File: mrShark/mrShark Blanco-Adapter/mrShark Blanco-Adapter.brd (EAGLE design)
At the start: 26 x 31 mm, 1 part, among them CON1 DF12-20DS

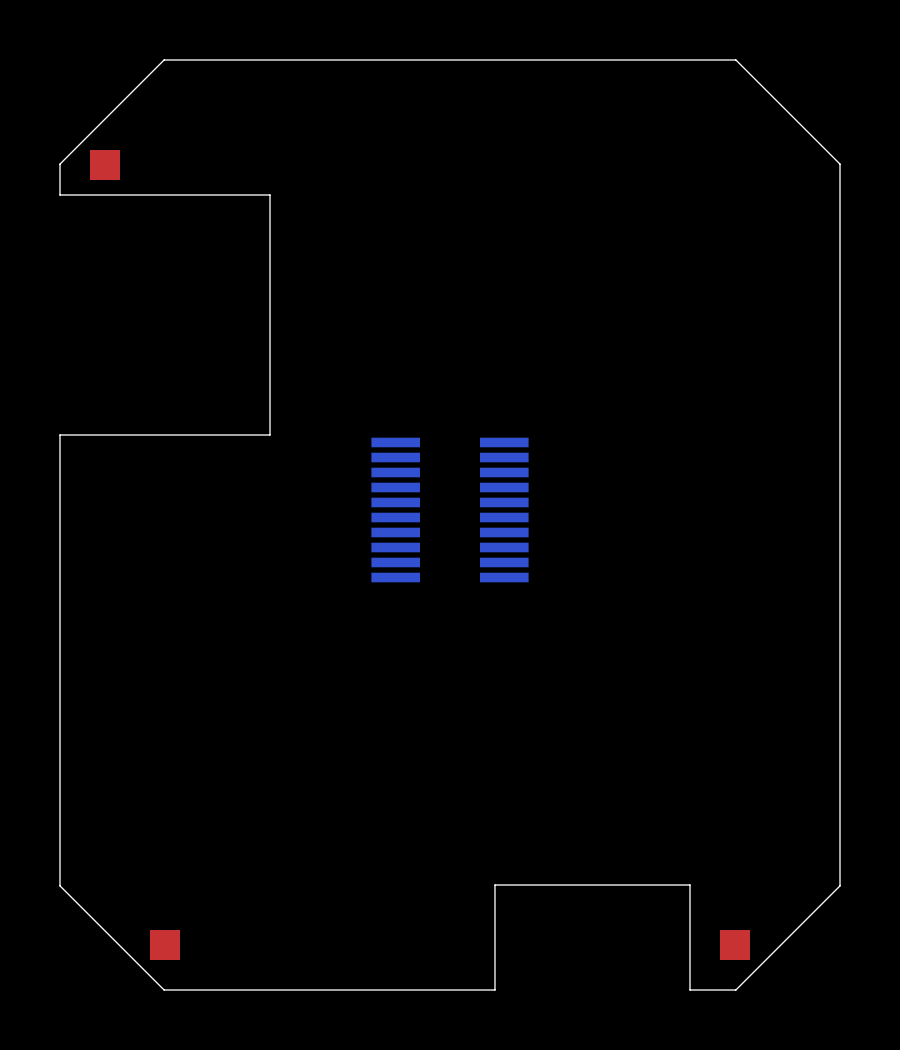
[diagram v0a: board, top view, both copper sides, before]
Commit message: Updated mrShark 1.2 & 1.3 Updated mrShark Adapter Updated mrShark LED-Marker to version 0.0.3
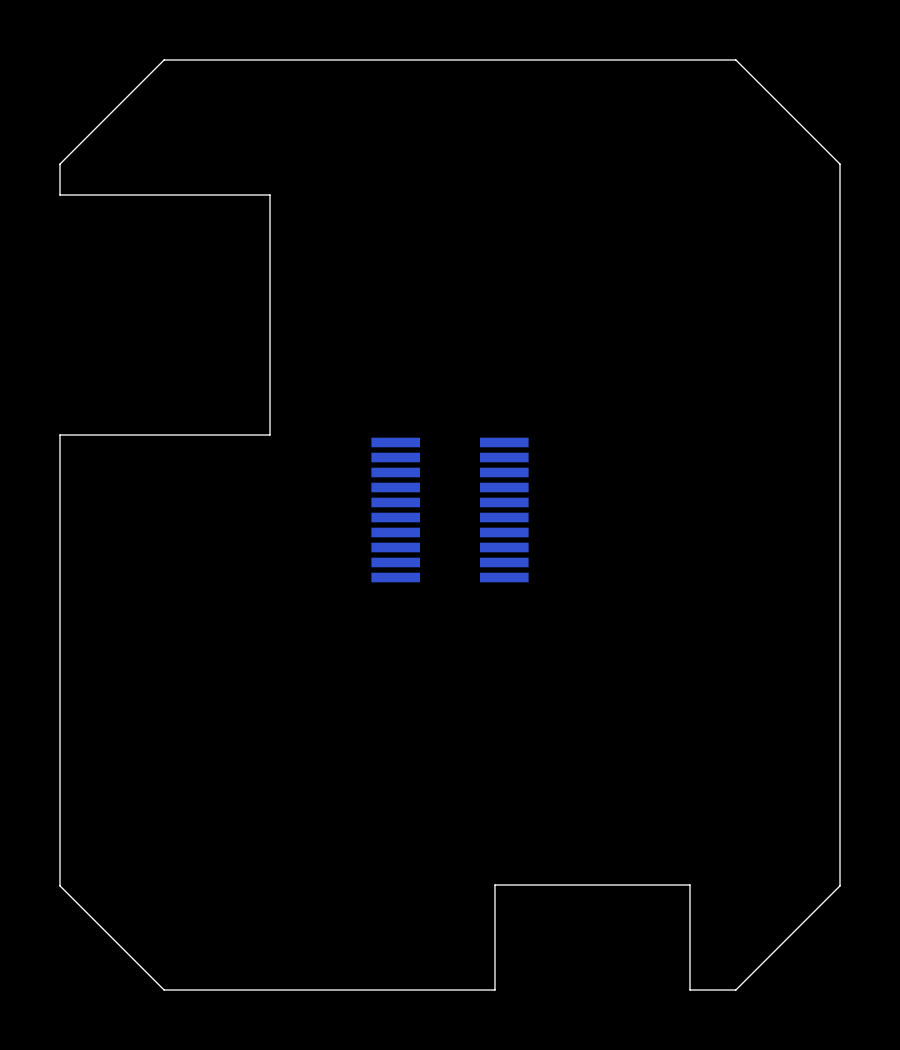
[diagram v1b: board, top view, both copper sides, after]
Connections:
- net GND: no longer CON1.16
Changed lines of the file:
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@@
 <?xml version="1.0" encoding="utf-8"?>
 <!DOCTYPE eagle SYSTEM "eagle.dtd">
-<eagle version="6.1">
+<eagle version="6.3">
 <drawing>
 <settings>
@@
 <wire x1="14.5" y1="3" x2="21" y2="3" width="0" layer="20"/>
 <wire x1="21" y1="3" x2="21" y2="-0.5" width="0" layer="20"/>
-<rectangle x1="1" y1="26.5" x2="2" y2="27.5" layer="16"/>
-<rectangle x1="1" y1="26.5" x2="2" y2="27.5" layer="1"/>
-<rectangle x1="22" y1="0.5" x2="23" y2="1.5" layer="1"/>
-<rectangle x1="22" y1="0.5" x2="23" y2="1.5" layer="16"/>
-<rectangle x1="3" y1="0.5" x2="4" y2="1.5" layer="16"/>
-<rectangle x1="3" y1="0.5" x2="4" y2="1.5" layer="1"/>
 </plain>
 <attributes>
@@
 </class>
 </classes>
-<designrules>
+<designrules name="default">
 <description language="de">&lt;b&gt;EAGLE Design Rules&lt;/b&gt;
 &lt;p&gt;
@@
 <signal name="GND">
 <contactref element="CON1" pad="15"/>
-<contactref element="CON1" pad="16"/>
 <contactref element="CON1" pad="12"/>
 <contactref element="CON1" pad="6"/>
-<wire x1="14.81" y1="15.25" x2="11.19" y2="15.25" width="0" layer="19" extent="16-16"/>
-<wire x1="14.81" y1="15.75" x2="14.81" y2="15.25" width="0" layer="19" extent="16-16"/>
 <wire x1="14.81" y1="13.75" x2="14.81" y2="15.25" width="0" layer="19" extent="16-16"/>
+<wire x1="11.19" y1="15.25" x2="14.81" y2="15.25" width="0" layer="19" extent="16-16"/>
 </signal>
 <signal name="INT1">
